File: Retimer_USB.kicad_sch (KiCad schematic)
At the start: 16 parts, among them IC1 PI2EQX22024XEAEX

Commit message: almost finished adding retimer for usb
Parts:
- IC1: footprint PI2EQX22024 -> PI2EQX22024:PI2EQX22024
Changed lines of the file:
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@@
 			)
 		)
-		(property "Footprint" "PI2EQX22024"
+		(property "Footprint" "PI2EQX22024:PI2EQX22024"
 			(at 88.9 131.75 0)
 			(effects

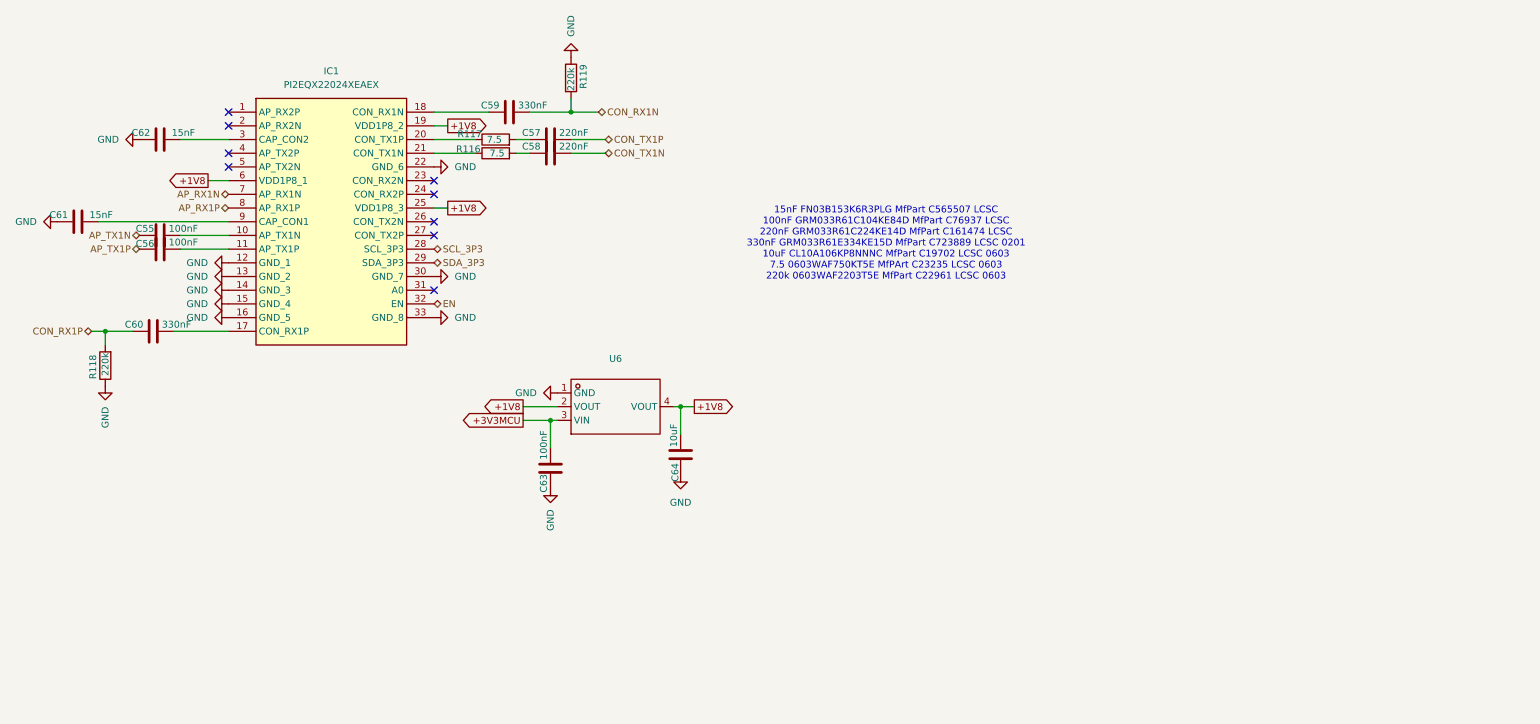
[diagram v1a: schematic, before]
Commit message: almost finished with implementing usb retimer
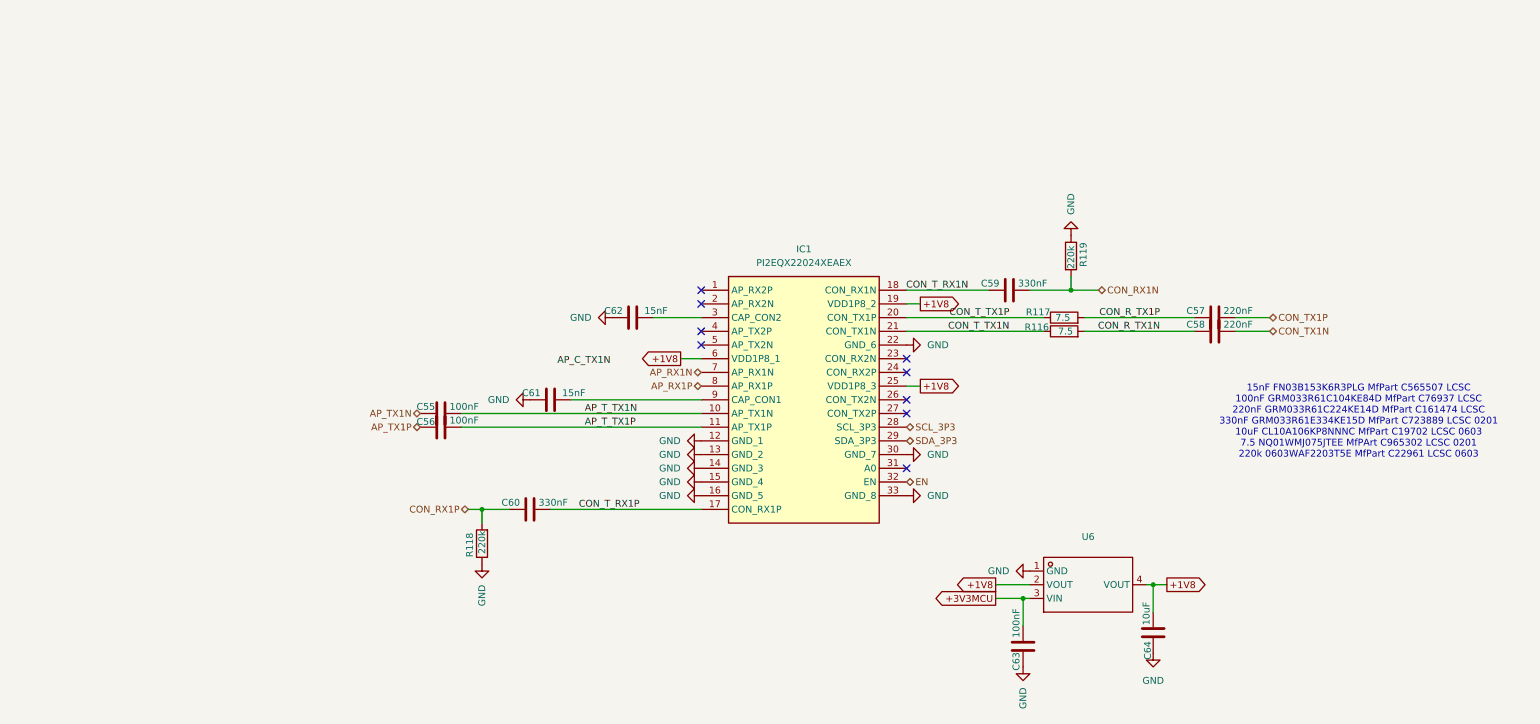
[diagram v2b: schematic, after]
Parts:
- R116, R117: footprint Resistor_SMD:R_0603_1608Metric -> Resistor_SMD:R_0201_0603Metric; LCSC C23235 -> C965302; Part_Number 0603WAF750KT5E -> NQ01WMJ075JTEE
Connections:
- net CON_R_TX1P: now reaches C57.2, R117.2
- net AP_T_TX1N: now reaches C55.1, IC1.10 (AP_TX1N)
- net AP_T_TX1P: now reaches C56.1, IC1.11 (AP_TX1P)
- net CON_T_RX1P: now reaches C60.1, IC1.17 (CON_RX1P)
- net CON_T_RX1N: now reaches C59.2, IC1.18 (CON_RX1N)
- net CON_T_TX1P: now reaches IC1.20 (CON_TX1P), R117.1
- net CON_T_TX1N: now reaches IC1.21 (CON_TX1N), R116.1
- net CON_R_TX1N: now reaches C58.2, R116.2
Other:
- note added: "15nF FN03B153K6R3PLG MfPart C565507 LCSC 100nF GRM033R61C104KE84D MfPart C76937 LCSC 220nF GRM033R61C224KE14D MfPart C161474 LCSC 330nF GRM033R61E334KE15D MfPart C723889 LCSC 0201 10uF CL10A106KP8NNNC MfPart C19702 LCSC 0603 7.5 NQ01WMJ075JTEE MfPArt C965302 LCSC 0201 220k 0603WAF2203T5E MfPart C22961 LCSC 0603"
- note removed: "15nF FN03B153K6R3PLG MfPart C565507 LCSC 100nF GRM033R61C104KE84D MfPart C76937 LCSC 220nF GRM033R61C224KE14D MfPart C161474 LCSC 330nF GRM033R61E334KE15D MfPart C723889 LCSC 0201 10uF CL10A106KP8NNNC MfPart C19702 LCSC 0603 7.5 0603WAF750KT5E MfPArt C23235 LCSC 0603 220k 0603WAF2203T5E MfPart C22961 LCSC 0603"
- moved on the sheet: C55, C56, C57, C58, C59, C60, C61, C62, C63, C64, IC1, R116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

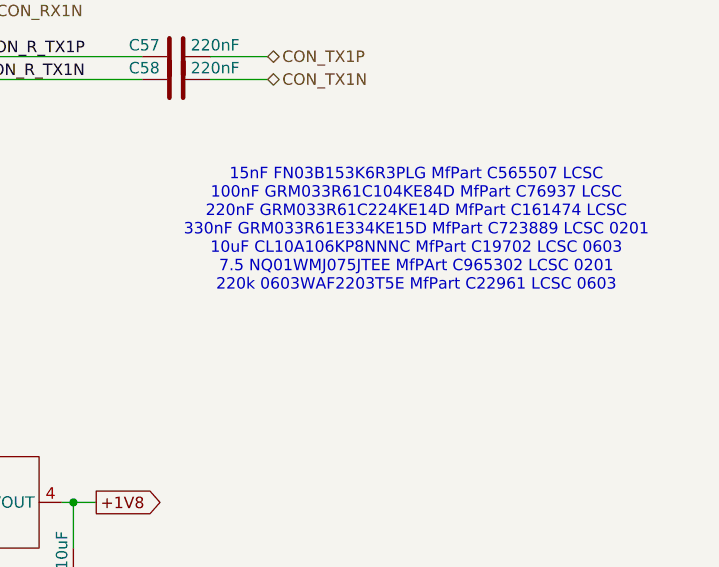
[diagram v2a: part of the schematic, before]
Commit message: finished usb retimer
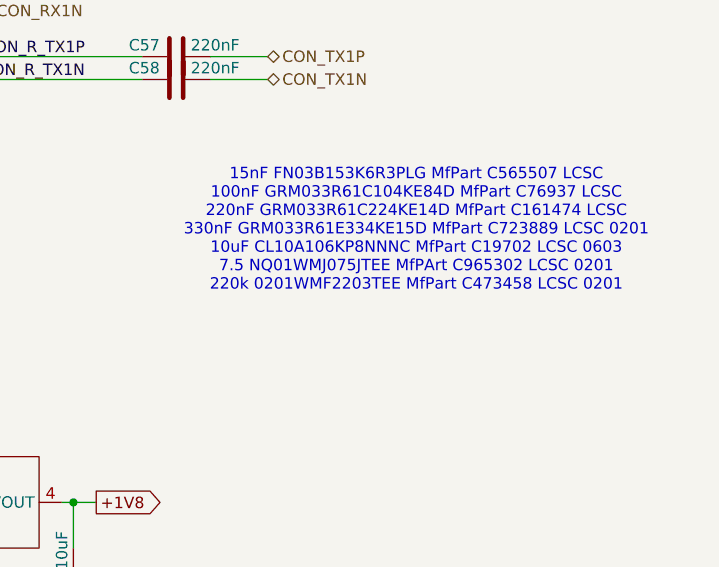
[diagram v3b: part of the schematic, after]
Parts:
- R118, R119: footprint Resistor_SMD:R_0603_1608Metric -> Resistor_SMD:R_0201_0603Metric; LCSC C22961 -> C473458; Part_Number 0603WAF2203T5E -> 0201WMF2203TEE
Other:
- note added: "15nF FN03B153K6R3PLG MfPart C565507 LCSC 100nF GRM033R61C104KE84D MfPart C76937 LCSC 220nF GRM033R61C224KE14D MfPart C161474 LCSC 330nF GRM033R61E334KE15D MfPart C723889 LCSC 0201 10uF CL10A106KP8NNNC MfPart C19702 LCSC 0603 7.5 NQ01WMJ075JTEE MfPArt C965302 LCSC 0201 220k 0201WMF2203TEE MfPart C473458 LCSC 0201"
- note removed: "15nF FN03B153K6R3PLG MfPart C565507 LCSC 100nF GRM033R61C104KE84D MfPart C76937 LCSC 220nF GRM033R61C224KE14D MfPart C161474 LCSC 330nF GRM033R61E334KE15D MfPart C723889 LCSC 0201 10uF CL10A106KP8NNNC MfPart C19702 LCSC 0603 7.5 NQ01WMJ075JTEE MfPArt C965302 LCSC 0201 220k 0603WAF2203T5E MfPart C22961 LCSC 0603"
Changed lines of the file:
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@@
 	(generator_version "9.0")
 	(paper "A4")
-	(text "15nF FN03B153K6R3PLG MfPart C565507 LCSC\n100nF GRM033R61C104KE84D MfPart C76937 LCSC\n220nF GRM033R61C224KE14D MfPart C161474 LCSC\n330nF GRM033R61E334KE15D MfPart C723889 LCSC 0201\n10uF CL10A106KP8NNNC MfPart C19702 LCSC 0603\n7.5 NQ01WMJ075JTEE MfPArt C965302 LCSC 0201\n220k 0603WAF2203T5E MfPart C22961 LCSC 0603"
+	(text "15nF FN03B153K6R3PLG MfPart C565507 LCSC\n100nF GRM033R61C104KE84D MfPart C76937 LCSC\n220nF GRM033R61C224KE14D MfPart C161474 LCSC\n330nF GRM033R61E334KE15D MfPart C723889 LCSC 0201\n10uF CL10A106KP8NNNC MfPart C19702 LCSC 0603\n7.5 NQ01WMJ075JTEE MfPArt C965302 LCSC 0201\n220k 0201WMF2203TEE MfPart C473458 LCSC 0201"
 		(exclude_from_sim no)
 		(at 264.16 94.234 0)
@@
 			)
 		)
-		(property "Footprint" "Resistor_SMD:R_0603_1608Metric"
+		(property "Footprint" "Resistor_SMD:R_0201_0603Metric"
 			(at 209.042 63.5 90)
 			(effects
@@
 			)
 		)
-		(property "LCSC" "C22961"
+		(property "LCSC" "C473458"
 			(at 210.82 63.5 0)
 			(effects
@@
 			)
 		)
-		(property "Part_Number" "0603WAF2203T5E"
+		(property "Part_Number" "0201WMF2203TEE"
 			(at 210.82 63.5 0)
 			(effects
@@
 			)
 		)
-		(property "Footprint" "Resistor_SMD:R_0603_1608Metric"
+		(property "Footprint" "Resistor_SMD:R_0201_0603Metric"
 			(at 103.378 116.84 90)
 			(effects
@@
 			)
 		)
-		(property "LCSC" "C22961"
+		(property "LCSC" "C473458"
 			(at 101.6 116.84 0)
 			(effects
@@
 			)
 		)
-		(property "Part_Number" "0603WAF2203T5E"
+		(property "Part_Number" "0201WMF2203TEE"
 			(at 101.6 116.84 0)
 			(effects

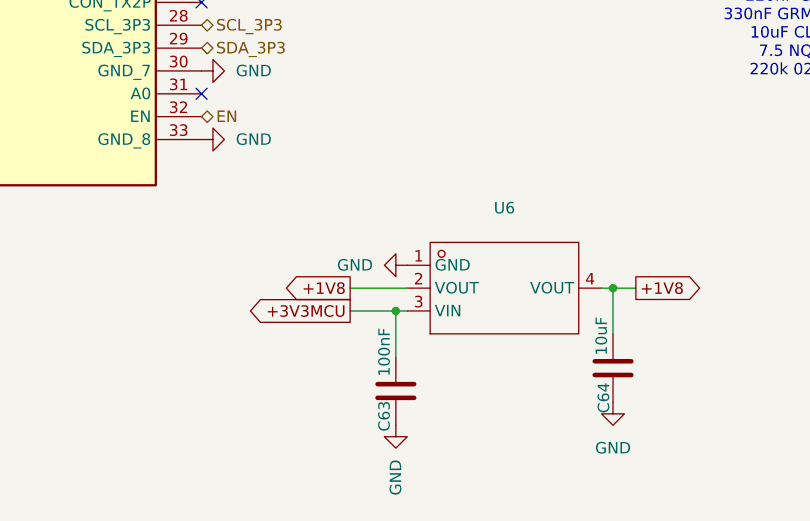
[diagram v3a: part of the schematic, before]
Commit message: added better ldo
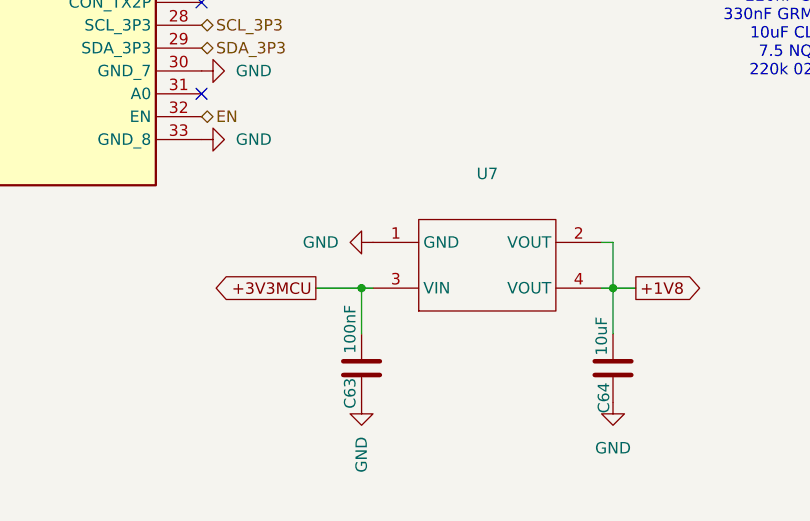
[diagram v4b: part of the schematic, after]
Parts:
- removed U6: ~, LD1117S18CTR:SOT-223-3_L6.5-W3.4-P2.30-LS7.0-BR, symbol LD1117S18CTR:LD1117S18CTR
- added U7: ~, LD1117S18TR:SOT-223_L6.5-W3.5-P2.30-LS7.0-BR, symbol LD1117S18TR:LD1117S18TR
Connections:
- net +1V8: now also U7.2 (VOUT), U7.4 (VOUT)
- net +3V3MCU: now also U7.3 (VIN)
- net GND: now also U7.1 (GND)
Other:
- moved on the sheet: C63
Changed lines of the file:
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@@
 	)
 	(junction
-		(at 201.93 127)
+		(at 198.12 124.46)
 		(diameter 0)
 		(color 0 0 0 0)
@@
 	(wire
 		(pts
-			(xy 196.85 124.46) (xy 203.2 124.46)
-		)
-		(stroke
-			(width 0)
-			(type default)
-		)
-	)
-	(wire
-		(pts
 			(xy 97.79 92.71) (xy 142.24 92.71)
 		)
@@
 	(wire
 		(pts
-			(xy 201.93 127) (xy 201.93 132.08)
+			(xy 198.12 124.46) (xy 198.12 129.54)
 		)
 		(stroke
@@
 	(wire
 		(pts
-			(xy 196.85 127) (xy 201.93 127)
+			(xy 193.04 124.46) (xy 198.12 124.46)
 		)
 		(stroke
@@
 	(wire
 		(pts
-			(xy 201.93 127) (xy 203.2 127)
+			(xy 198.12 124.46) (xy 199.39 124.46)
+		)
+		(stroke
+			(width 0)
+			(type default)
+		)
+	)
+	(wire
+		(pts
+			(xy 224.79 119.38) (xy 226.06 119.38)
 		)
 		(stroke
@@
 	(wire
 		(pts
+			(xy 226.06 119.38) (xy 226.06 124.46)
+		)
+		(stroke
+			(width 0)
+			(type default)
+		)
+	)
+	(wire
+		(pts
 			(xy 241.3 77.47) (xy 247.65 77.47)
 		)
@@
 	(global_label "+3V3MCU"
 		(shape output)
-		(at 196.85 127 180)
+		(at 193.04 124.46 180)
 		(fields_autoplaced yes)
 		(effects
@@
 		)
 		(property "Intersheetrefs" "${INTERSHEET_REFS}"
-			(at 184.7329 127 0)
+			(at 180.9229 124.46 0)
 			(effects
 				(font
@@
 	(global_label "+1V8"
 		(shape output)
-		(at 196.85 124.46 180)
-		(fields_autoplaced yes)
-		(effects
-			(font
-				(size 1.27 1.27)
-			)
-			(justify right)
-		)
-		(property "Intersheetrefs" "${INTERSHEET_REFS}"
-			(at 188.7848 124.46 0)
-			(effects
-				(font
-					(size 1.27 1.27)
-				)
-				(justify right)
-				(hide yes)
-			)
-		)
-	)
-	(global_label "+1V8"
-		(shape output)
 		(at 182.88 72.39 0)
 		(fields_autoplaced yes)
@@
 	(symbol
 		(lib_id "power:GND")
-		(at 203.2 121.92 270)
+		(at 199.39 119.38 270)
 		(mirror x)
 		(unit 1)
@@
 		(dnp no)
 		(property "Reference" "#PWR0157"
-			(at 196.85 121.92 0)
+			(at 193.04 119.38 0)
 			(effects
 				(font
@@
 		)
 		(property "Value" "GND"
-			(at 199.39 121.9201 90)
+			(at 195.58 119.3801 90)
 			(effects
 				(font
@@
 		)
 		(property "Footprint" ""
-			(at 203.2 121.92 0)
+			(at 199.39 119.38 0)
 			(effects
 				(font
@@
 		)
 		(property "Datasheet" ""
-			(at 203.2 121.92 0)
+			(at 199.39 119.38 0)
 			(effects
 				(font
@@
 		)
 		(property "Description" "Power symbol creates a global label with name \"GND\" , ground"
-			(at 203.2 121.92 0)
+			(at 199.39 119.38 0)
 			(effects
 				(font
@@
 	)
 	(symbol
+		(lib_id "LD1117S18TR:LD1117S18TR")
+		(at 212.09 121.92 0)
+		(unit 1)
+		(exclude_from_sim no)
+		(in_bom yes)
+		(on_board yes)
+		(dnp no)
+		(fields_autoplaced yes)
+		(property "Reference" "U7"
+			(at 212.09 111.76 0)
+			(effects
+				(font
+					(size 1.27 1.27)
+				)
+			)
+		)
+		(property "Value" "~"
+			(at 212.09 114.3 0)
+			(effects
+				(font
+					(size 1.27 1.27)
+				)
+			)
+		)
+		(property "Footprint" "LD1117S18TR:SOT-223_L6.5-W3.5-P2.30-LS7.0-BR"
+			(at 212.09 121.92 0)
+			(effects
+				(font
+					(size 1.27 1.27)
+				)
+				(hide yes)
+			)
+		)
+		(property "Datasheet" "https://atta.szlcsc.com/upload/public/pdf/source/20181022/C283467_00098992BB1D287195B66486CE33A2DD.pdf"
+			(at 212.09 121.92 0)
+			(effects
+				(font
+					(size 1.27 1.27)
+				)
+				(hide yes)
+			)
+		)
+		(property "Description" "Output Type:Fixed Maximum Input Voltage:15V Output Voltage:1.8V Output Voltage:1.8V Output Current:800mA Power Supply Rejection Ratio (PSRR):75dB@(120Hz) Dropout Voltage:1.2V@(800mA) standby current:10mA Feature:Thermal Protection(TSD)；Overcurrent Protect"
+			(at 212.09 121.92 0)
+			(effects
+				(font
+					(size 1.27 1.27)
+				)
+				(hide yes)
+			)
+		)
+		(property "Part_Number" "LD1117S18TR"
+			(at 212.09 121.92 0)
+			(effects
+				(font
+					(size 1.27 1.27)
+				)
+				(hide yes)
+			)
+		)
+		(property "LCSC" "C80598"
+			(at 212.09 121.92 0)
+			(effects
+				(font
+					(size 1.27 1.27)
+				)
+				(hide yes)
+			)
+		)
+		(pin "3"
+		)
+		(pin "4"
+		)
+		(pin "1"
+		)
+		(pin "2"
+		)
+		(instances
+			(project ""
+				(path "/f97e6956-ab08-42cb-8fed-03fa58e87f0e/a254375d-80c0-4b18-9fd6-3cbd6a868414"
+					(reference "U7")
+					(unit 1)
+				)
+			)
+		)
+	)
+	(symbol
 		(lib_id "Device:C")
 		(at 199.39 69.85 270)
@@
 	(symbol
 		(lib_id "Device:C")
-		(at 201.93 135.89 0)
+		(at 198.12 133.35 0)
 		(unit 1)
 		(exclude_from_sim no)
@@
 		(dnp no)
 		(property "Reference" "C63"
-			(at 200.66 138.684 90)
+			(at 196.85 136.144 90)
 			(effects
 				(font
@@
 		)
 		(property "Value" "100nF"
-			(at 200.66 131.572 90)
+			(at 196.85 129.032 90)
 			(effects
 				(font
@@
 		)
 		(property "Footprint" "Capacitor_SMD:C_0201_0603Metric"
-			(at 202.8952 139.7 0)
+			(at 199.0852 137.16 0)
 			(effects
 				(font
@@
 		)
 		(property "Datasheet" "~"
-			(at 201.93 135.89 0)
+			(at 198.12 133.35 0)
 			(effects
 				(font
@@
 		)
 		(property "Description" "Unpolarized capacitor"
-			(at 201.93 135.89 0)
+			(at 198.12 133.35 0)
 			(effects
 				(font
@@
 		)
 		(property "Part_Number" "GRM033R61C104KE84D"
-			(at 201.93 135.89 0)
+			(at 198.12 133.35 0)
 			(effects
 				(font
@@
 		)
 		(property "LCSC" "C76937"
-			(at 201.93 135.89 0)
+			(at 198.12 133.35 0)
 			(effects
 				(font
@@
 	)
 	(symbol
-		(lib_id "LD1117S18CTR:LD1117S18CTR")
-		(at 214.63 124.46 0)
-		(unit 1)
-		(exclude_from_sim no)
-		(in_bom yes)
-		(on_board yes)
-		(dnp no)
-		(fields_autoplaced yes)
-		(property "Reference" "U6"
-			(at 213.995 115.57 0)
-			(effects
-				(font
-					(size 1.27 1.27)
-				)
-			)
-		)
-		(property "Value" "~"
-			(at 213.995 118.11 0)
-			(effects
-				(font
-					(size 1.27 1.27)
-				)
-			)
-		)
-		(property "Footprint" "LD1117S18CTR:SOT-223-3_L6.5-W3.4-P2.30-LS7.0-BR"
-			(at 214.63 124.46 0)
-			(effects
-				(font
-					(size 1.27 1.27)
-				)
-				(hide yes)
-			)
-		)
-		(property "Datasheet" "https://item.szlcsc.com/datasheet/LD1117S18CTR/703436.html"
-			(at 214.63 124.46 0)
-			(effects
-				(font
-					(size 1.27 1.27)
-				)
-				(hide yes)
-			)
-		)
-		(property "Description" "Output Type:Fixed Voltage - Supply:15V Output Voltage:1.8V Output Voltage:1.8V Output Current:800mA Power Supply Rejection Ratio (PSRR):75dB@(120Hz) Voltage Dropout:1.3V@(800mA) standby current:10mA Noise:100uV Features:Over Current Protection Operating T"
-			(at 214.63 124.46 0)
-			(effects
-				(font
-					(size 1.27 1.27)
-				)
-				(hide yes)
-			)
-		)
-		(property "Part_Number" "LD1117S18CTR"
-			(at 214.63 124.46 0)
-			(effects
-				(font
-					(size 1.27 1.27)
-				)
-				(hide yes)
-			)
-		)
-		(property "LCSC" "C672391"
-			(at 214.63 124.46 0)
-			(effects
-				(font
-					(size 1.27 1.27)
-				)
-				(hide yes)
-			)
-		)
-		(pin "4"
-		)
-		(pin "2"
-		)
-		(pin "3"
-		)
-		(pin "1"
-		)
-		(instances
-			(project ""
-				(path "/f97e6956-ab08-42cb-8fed-03fa58e87f0e/a254375d-80c0-4b18-9fd6-3cbd6a868414"
-					(reference "U6")
-					(unit 1)
-				)
-			)
-		)
-	)
-	(symbol
 		(lib_id "power:GND")
 		(at 142.24 100.33 270)
@@
 	(symbol
 		(lib_id "power:GND")
-		(at 201.93 139.7 0)
+		(at 198.12 137.16 0)
 		(mirror y)
 		(unit 1)
@@
 		(dnp no)
 		(property "Reference" "#PWR0160"
-			(at 201.93 146.05 0)
+			(at 198.12 143.51 0)
 			(effects
 				(font
@@
 		)
 		(property "Value" "GND"
-			(at 201.9301 143.51 90)
+			(at 198.1201 140.97 90)
 			(effects
 				(font
@@
 		)
 		(property "Footprint" ""
-			(at 201.93 139.7 0)
+			(at 198.12 137.16 0)
 			(effects
 				(font
@@
 		)
 		(property "Datasheet" ""
-			(at 201.93 139.7 0)
+			(at 198.12 137.16 0)
 			(effects
 				(font
@@
 		)
 		(property "Description" "Power symbol creates a global label with name \"GND\" , ground"
-			(at 201.93 139.7 0)
+			(at 198.12 137.16 0)
 			(effects
 				(font
